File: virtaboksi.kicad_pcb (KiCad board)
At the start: 2 copper layers, 50 x 71.9 mm, 62 parts, among them J1 Optional_01x03, J2 Ext_01x05, J3 Optional_01x02_Male, J4 Panel_01x08, J5 Powerpole 01x02, J6 Powerpole 01x02, J7 Powerpole 01x02, J8 TagConnect_TC2030-NL, Q1 2N7002, Q2 IRF4905, Q3 IRF4905, Q4 2N7002, Q5 IRF4905, Q6 IRF4905, Q7 2N7002, Q8 IRF4905, Q9 IRF4905, U1 SRV05-4, U2 AMSRI-783.3-NZ, U3 SRV05-4, U4 SP3485EN, U5 STM8S003F3P

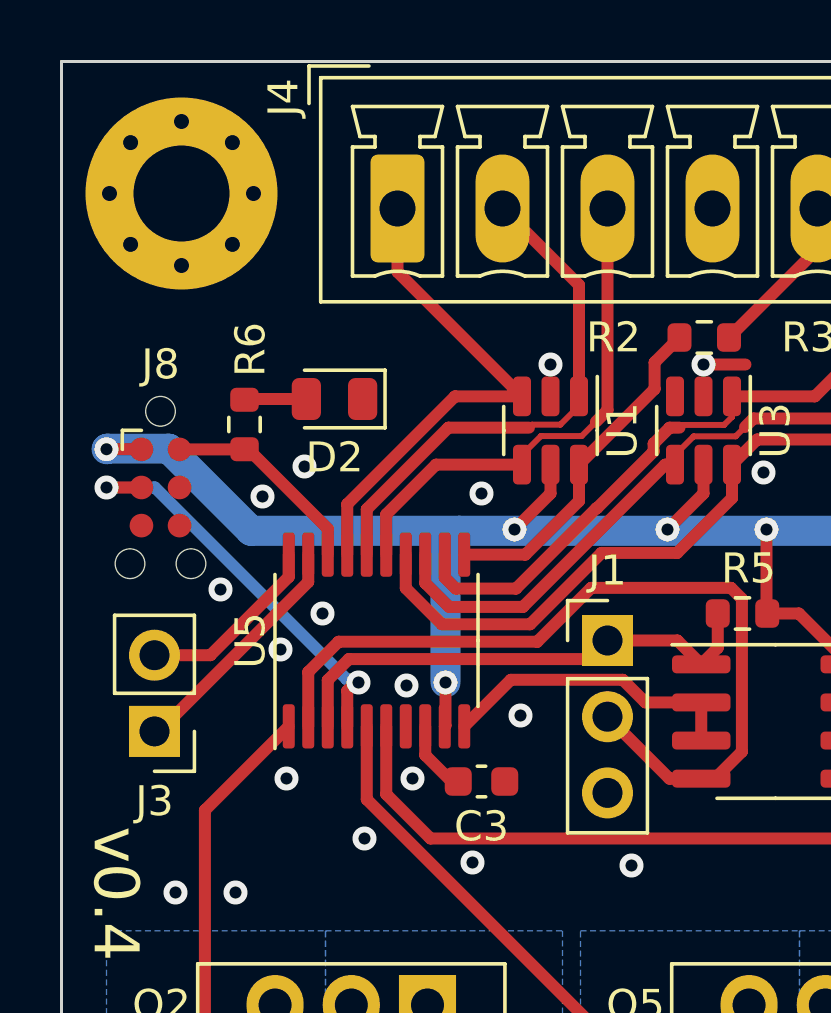
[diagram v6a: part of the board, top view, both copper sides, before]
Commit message: Rename connectors J1-J4
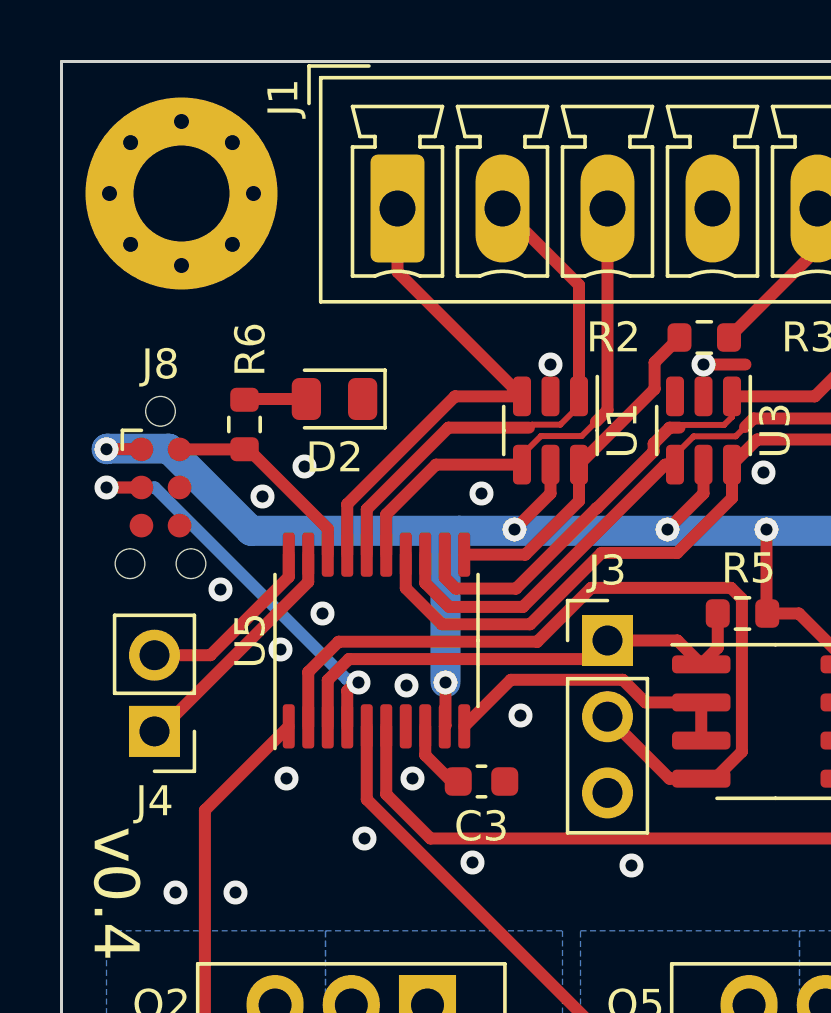
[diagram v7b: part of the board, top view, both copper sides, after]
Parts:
- renumbered J4 to J1, J1 to J3, J3 to J4

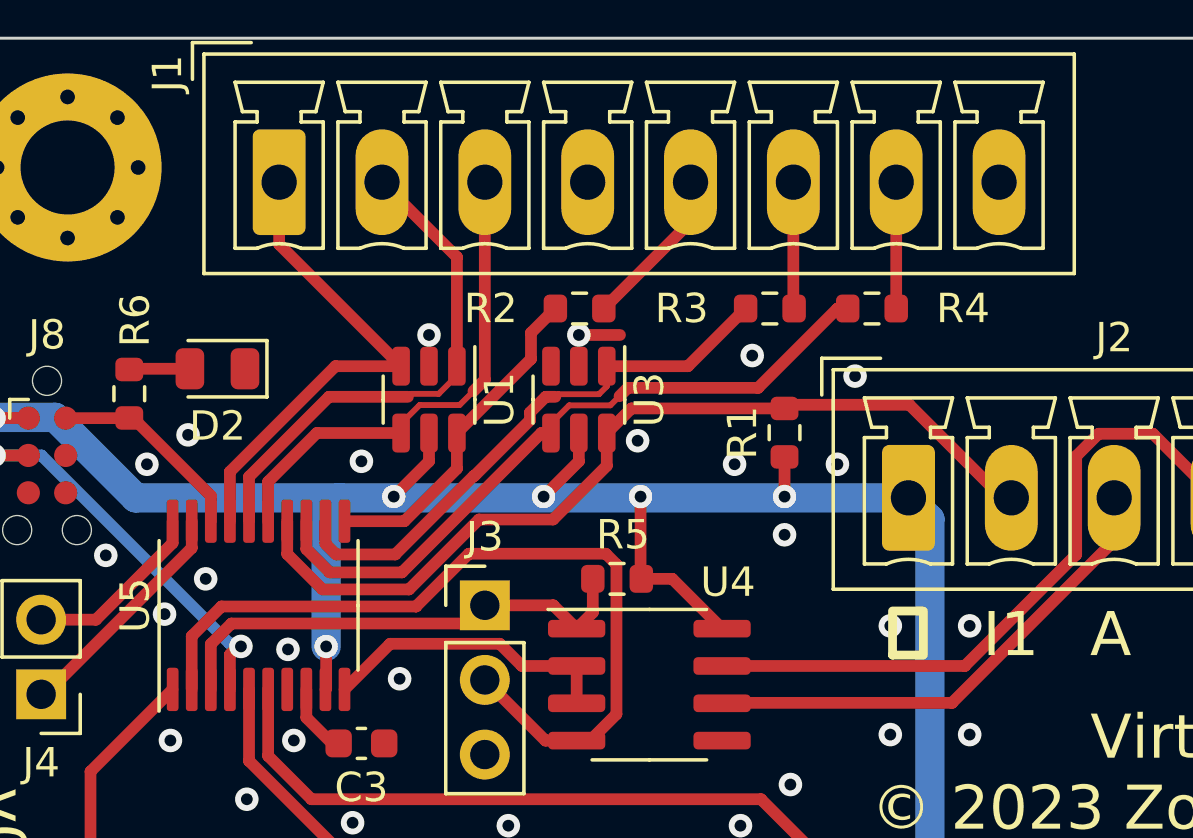
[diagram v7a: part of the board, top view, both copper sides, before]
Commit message: Add stronger pull-ups for inputs
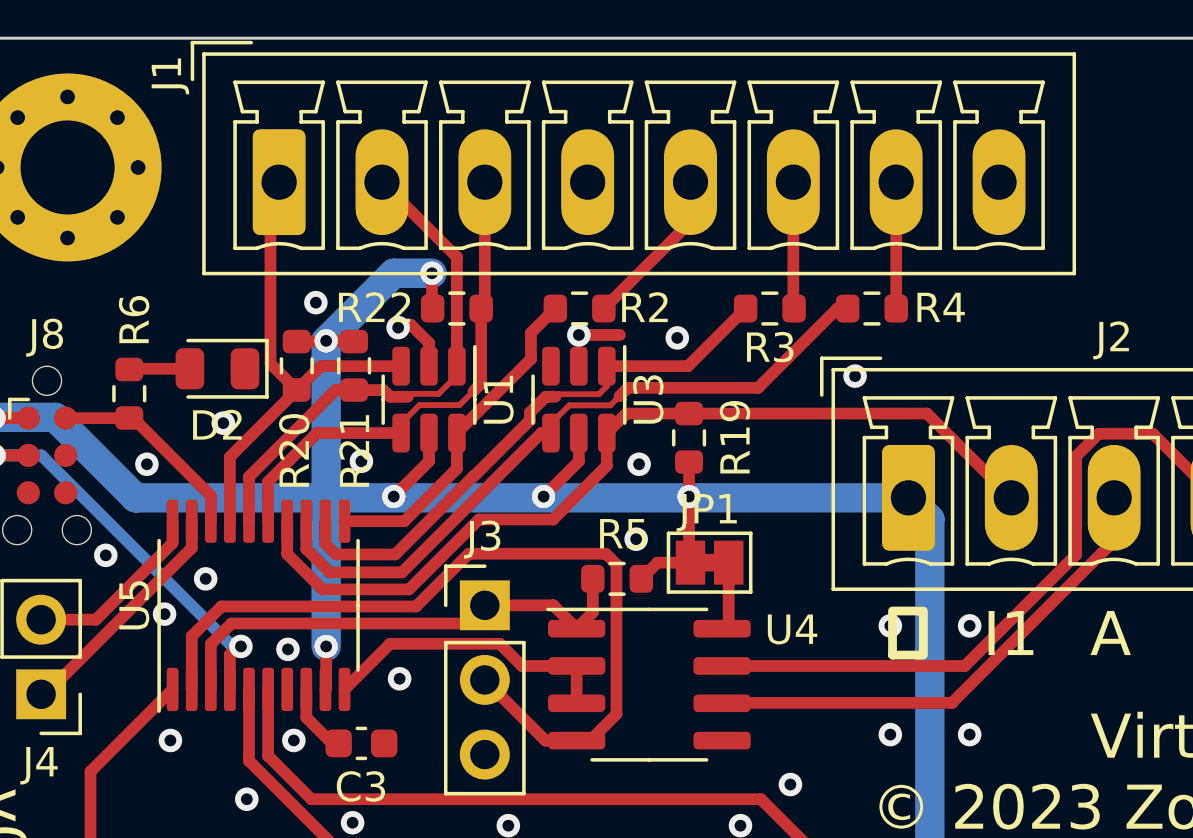
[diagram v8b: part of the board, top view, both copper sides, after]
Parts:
- added JP1: SolderJumper_2_Bridged, Jumper:SolderJumper-2_P1.3mm_Bridged_Pad1.0x1.5mm, F.Cu at (133.3, 57.9)
- added R20: 5k, Resistor_SMD:R_0603_1608Metric, F.Cu at (119.3, 51.1)
- added R21: 5k, Resistor_SMD:R_0603_1608Metric, F.Cu at (121.2, 51.1)
- added R22: 5k, Resistor_SMD:R_0603_1608Metric, F.Cu at (124.8, 49.2)
- R19: renamed from R1; value 2k -> 5k
- moved R19 3.25 mm to (132.7, 53.6)
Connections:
- U4 pad 8: +3.3V -> Net-(JP1-Pad2)
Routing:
- net +3.3V: track 116.7 -> 127.4 mm, vias 6 -> 7
- net Net-(JP1-Pad2): track 0.00 -> 2.34 mm
- net GND: track 1.40 -> 3.50 mm, vias 33 -> 32
- net /IN1: track 30.1 -> 30.6 mm
